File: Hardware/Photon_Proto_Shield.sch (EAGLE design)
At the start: 13 parts

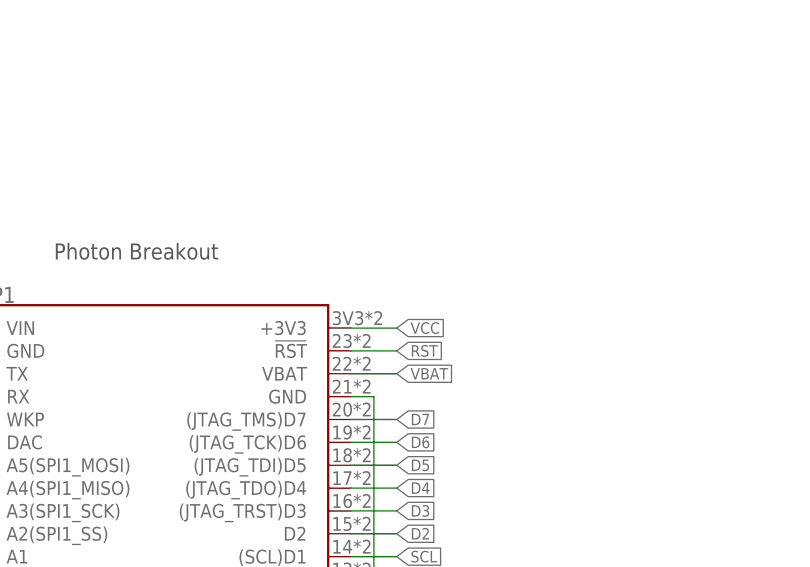
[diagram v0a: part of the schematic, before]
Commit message: Change VCC from flag label to VCC symbol
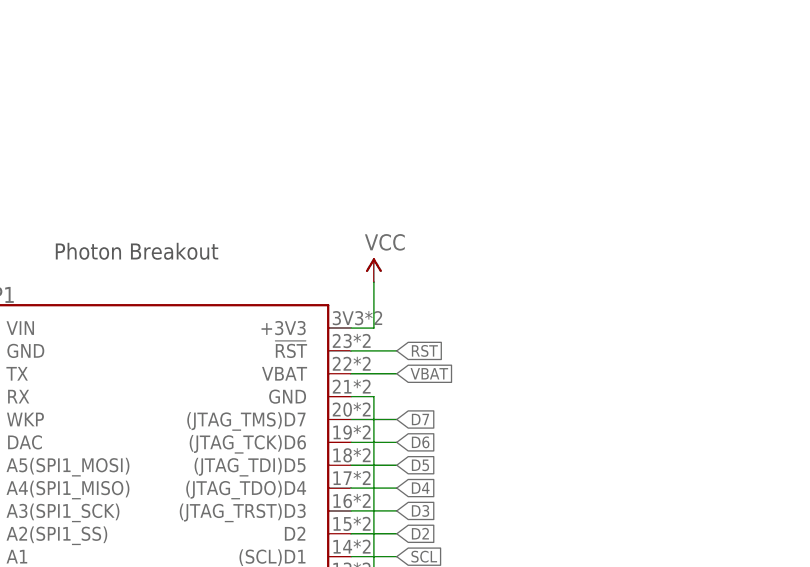
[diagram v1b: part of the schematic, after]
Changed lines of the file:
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@@
 <part name="JP10" library="SparkFun-Connectors" deviceset="M09" device="NO_SILK"/>
 <part name="LOGO1" library="SparkFun-Aesthetics" deviceset="SFE_LOGO_NAME_FLAME" device=".1_INCH"/>
+<part name="SUPPLY3" library="SparkFun-Aesthetics" deviceset="VCC" device=""/>
 </parts>
 <sheets>
@@
 <instance part="JP10" gate="G$1" x="226.06" y="91.44"/>
 <instance part="LOGO1" gate="G$1" x="2.54" y="2.54"/>
+<instance part="SUPPLY3" gate="G$1" x="93.98" y="129.54"/>
 </instances>
 <busses>
@@
 <segment>
 <pinref part="JP1" gate="G$1" pin="+3V3"/>
-<wire x1="91.44" y1="124.46" x2="96.52" y2="124.46" width="0.1524" layer="91"/>
-<label x="96.52" y="124.46" size="1.27" layer="95" xref="yes"/>
-</segment>
-<segment>
+<wire x1="91.44" y1="124.46" x2="93.98" y2="124.46" width="0.1524" layer="91"/>
+<wire x1="93.98" y1="124.46" x2="93.98" y2="129.54" width="0.1524" layer="91"/>
+<pinref part="SUPPLY3" gate="G$1" pin="VCC"/>
+</segment>
+<segment>
